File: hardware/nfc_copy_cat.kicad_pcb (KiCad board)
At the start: 2 copper layers, 40.4 x 43 mm, 41 parts, among them J1 USB_B_Micro, J2 Battery, J3 SWD, J4 NFC Module V3, J5 Conn_01x02, J6 Adafruit NFC 1.0, SW1 RST, SW2 Magspoof, SW3 NFC, U1 AP2112K-3.3TRG1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

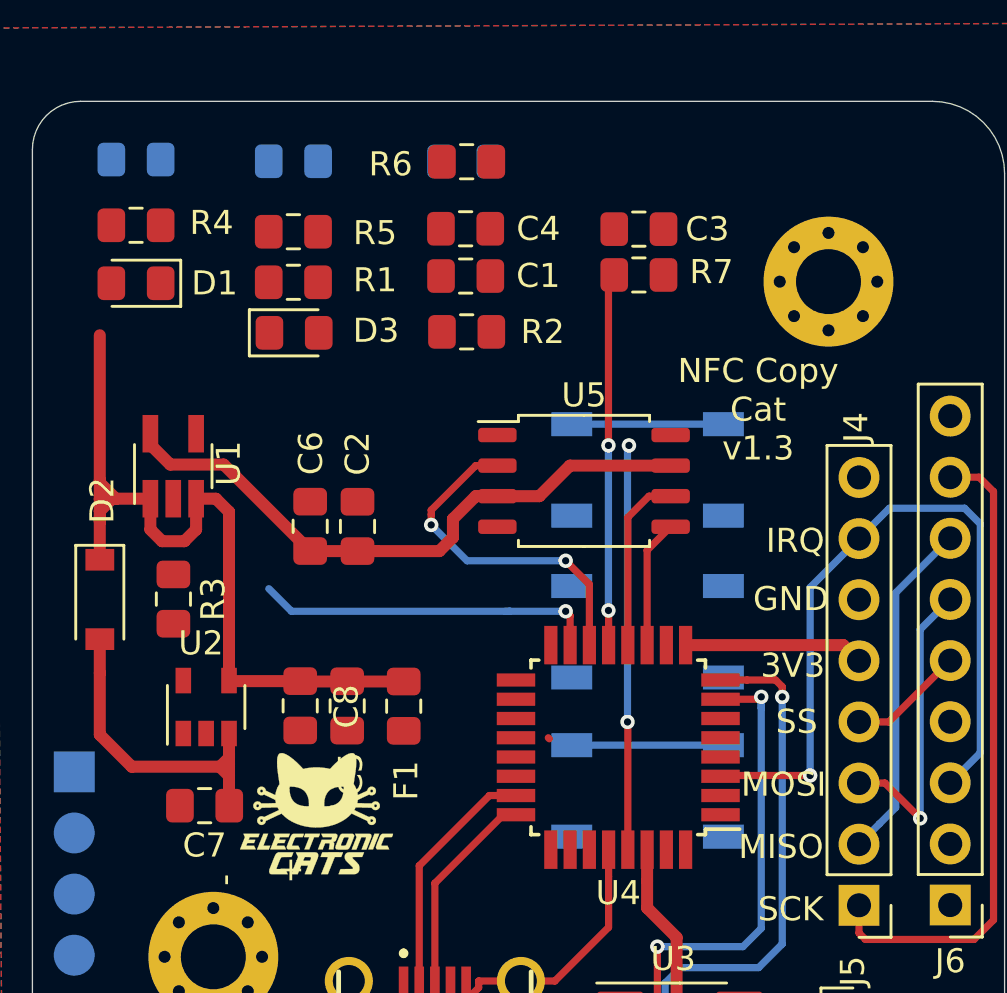
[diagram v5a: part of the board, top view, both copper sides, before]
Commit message: change led 1, res and push
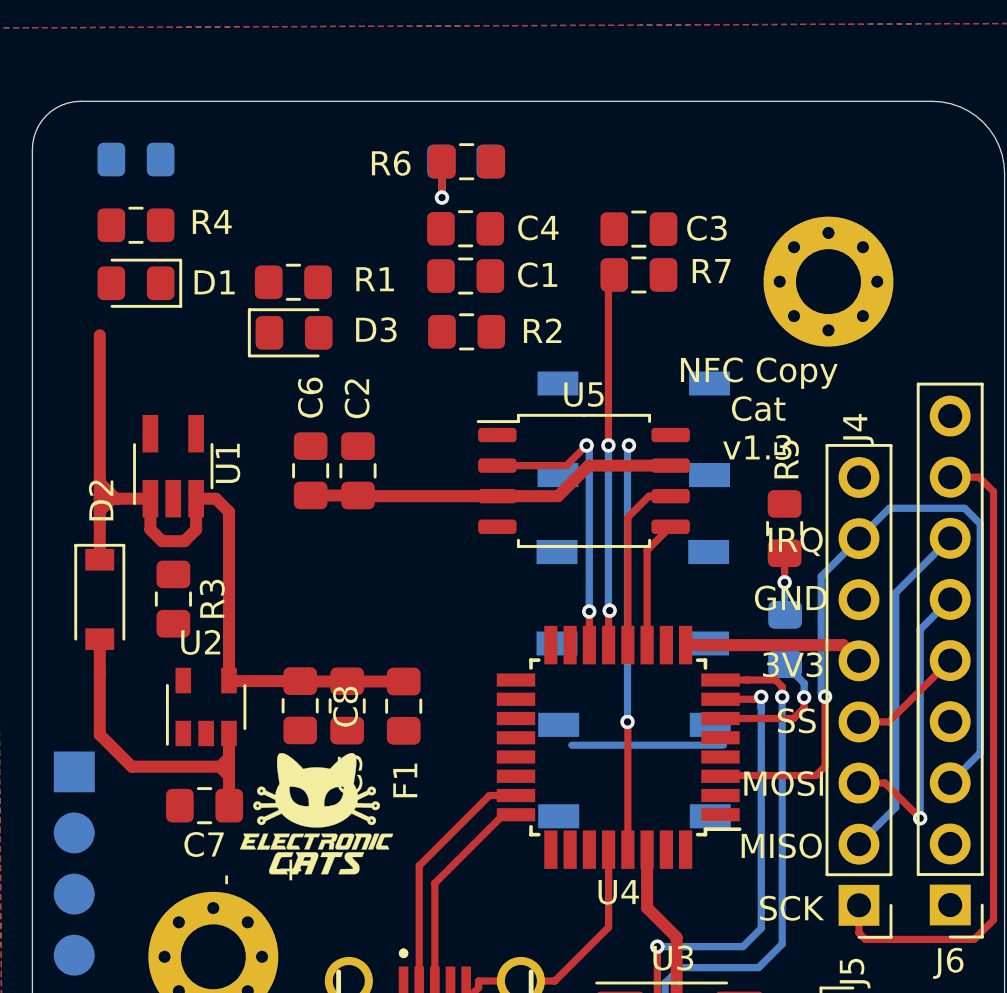
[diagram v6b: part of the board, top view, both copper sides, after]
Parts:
- moved D5 28.5 mm to (159.0, 71.6), turned to 270 degrees
- moved R5 23.9 mm to (159.0, 67.0), turned to 90 degrees
- moved C6 2.31 mm to (139.3, 64.6)
- moved C2 2.31 mm to (141.2, 64.6)
- moved SW3 1.78 mm to (152.7, 62.8)
- moved SW2 1.54 mm to (152.7, 69.8)
- moved SW1 1.01 mm to (152.7, 77.0)
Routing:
- net /LED1: track 14.4 -> 0.00 mm, vias 1 -> 0
- net +3V3: track 44.3 -> 33.9 mm
- net /SW2: track 6.30 -> 0.00 mm
- net /LED2: track 0.00 -> 5.80 mm, vias 0 -> 1
- net Net-(D6-Pad1): track 0.00 -> 3.01 mm, vias 0 -> 1
- net Net-(D5-Pad1): track 0.00 -> 2.57 mm, vias 0 -> 1
- net /MISO: track 14.2 -> 12.4 mm

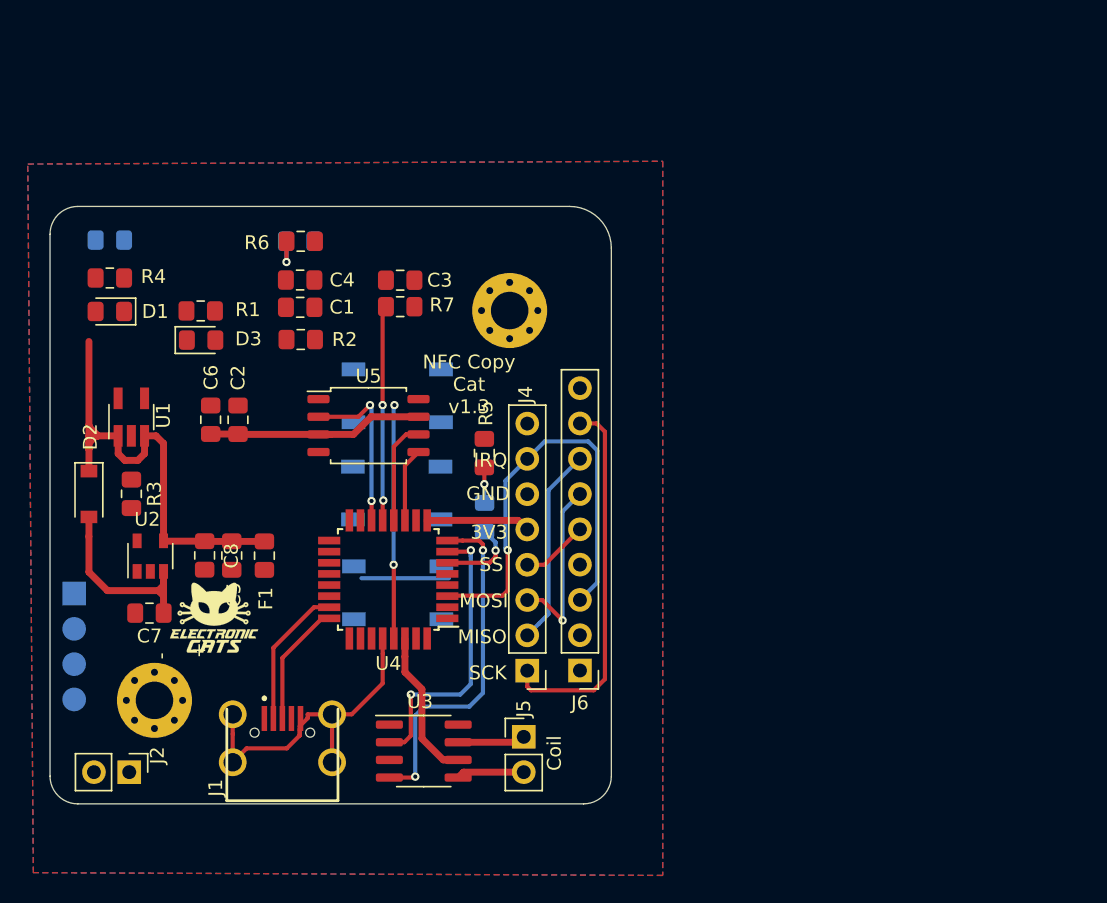
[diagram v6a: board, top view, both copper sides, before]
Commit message: routeo 3v and samd
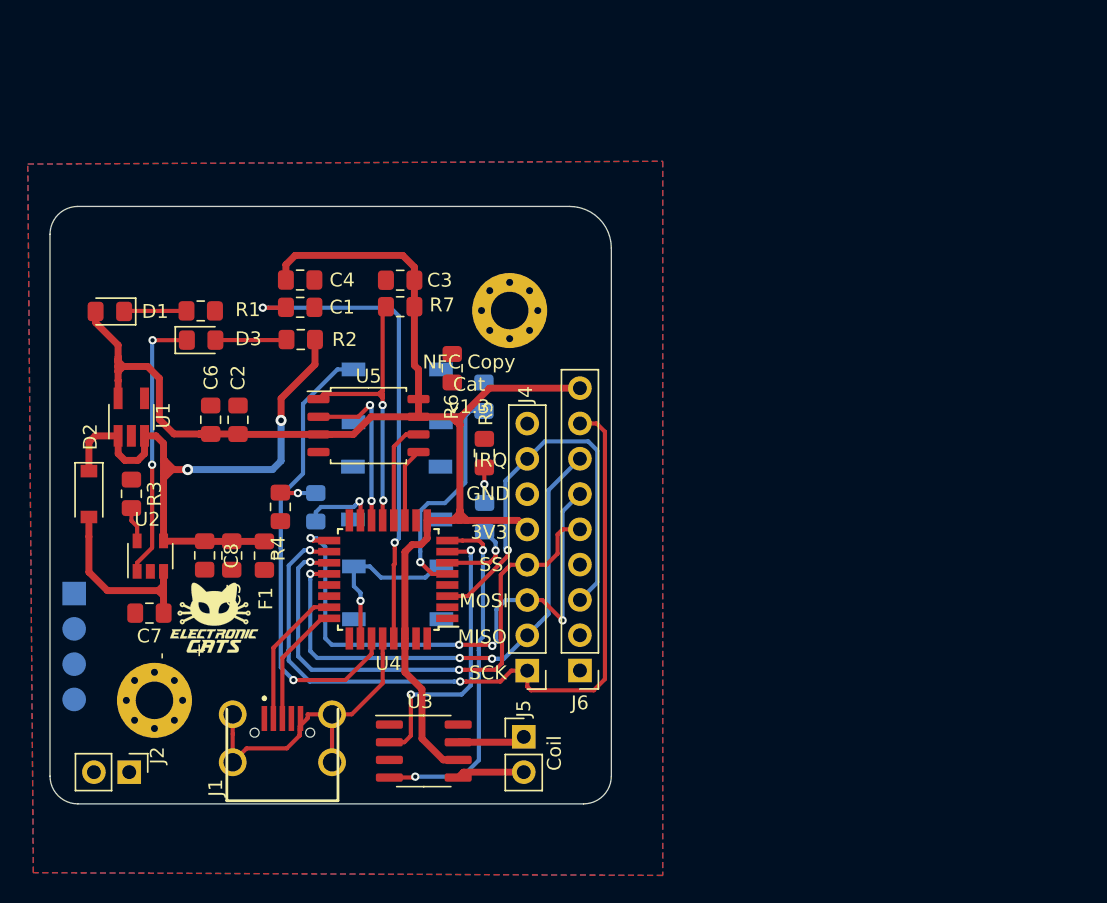
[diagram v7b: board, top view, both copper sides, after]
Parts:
- moved D4 24.3 mm to (146.8, 70.9), turned to 270 degrees
- moved R4 20.5 mm to (144.3, 70.8), turned to 270 degrees
- moved D6 17.3 mm to (158.9, 62.9), turned to 270 degrees
- moved R6 14.2 mm to (156.7, 60.8), turned to 90 degrees
- moved G*** 4.44 mm to (139.4, 71.8)
- moved REF** 3.82 mm to (139.1, 64.1)
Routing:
- net +3V3: track 33.9 -> 109.1 mm
- net /10(SS): track 4.85 -> 38.5 mm, vias 0 -> 2
- net /SW2: track 0.00 -> 33.2 mm, vias 0 -> 1
- net /13(SCK): track 27.0 -> 55.6 mm, vias 0 -> 2
- net /11(MOSI): track 12.8 -> 39.6 mm, vias 1 -> 4
- net /12(MISO): track 14.3 -> 37.8 mm, vias 0 -> 3
- net Net-(D3-Pad1): track 0.00 -> 19.6 mm, vias 0 -> 2
- net Net-(C1-Pad1): track 16.8 -> 35.1 mm
- net /LED3: track 0.00 -> 16.4 mm, vias 0 -> 1
- net VCC: track 35.1 -> 46.4 mm, vias 0 -> 2
- net /RESET: track 6.30 -> 12.4 mm, vias 0 -> 1
- net /SS: track 15.5 -> 21.2 mm
- net /LED1: track 0.00 -> 5.55 mm, vias 0 -> 1
- net Net-(D3-Pad2): track 0.00 -> 5.14 mm
- net Net-(D1-Pad1): track 0.00 -> 4.51 mm
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
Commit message: routeo reset and usb
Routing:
- net Net-(F1-Pad2): track 0.00 -> 10.7 mm
- net /SW1: track 0.00 -> 9.58 mm, vias 0 -> 2
- net /SS: track 21.2 -> 22.8 mm
- net /IRQ: track 30.4 -> 31.0 mm
- net Net-(C1-Pad1): track 35.1 -> 35.6 mm
